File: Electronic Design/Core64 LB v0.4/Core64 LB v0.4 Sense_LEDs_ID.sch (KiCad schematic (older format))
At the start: 18 parts, among them J6 Conn_01x08_Female, U3 LM393, U5 74HC02, U7 LM393

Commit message: Update schematic
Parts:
- added C4, C5: 0.1uF, Capacitor_SMD:C_0805_2012Metric, symbol Device:C
- added J10: TSM-106-03-T-DV‎, Connector_PinHeader_2.54mm:PinHeader_2x07_P2.54mm_Vertical_SMD_and_TH, symbol Connector_Generic:Conn_02x07_Odd_Even
- added J17: LED Cur. Mon., Connector_PinSocket_2.54mm:PinSocket_1x02_P2.54mm_Vertical, symbol Connector_Generic:Conn_01x02
- added R50: 470, Resistor_SMD:R_0805_2012Metric, symbol Device:R
- added U3: SN74LV1T125DBVR, Package_TO_SOT_SMD:SOT-23-5, symbol Logic_LevelTranslator:SN74LV1T125DBVR
- added U4: M24C01-RMN, Package_SO:SOIC-8_3.9x4.9mm_P1.27mm, symbol Memory_EEPROM:M24C01-RMN
- J6: value Conn_01x08_Female -> HEADER_8-PIN_0.1
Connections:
- net 3V3: now also C5.1, U4.1 (E0), U4.2 (E1), U4.3 (E2), U4.8 (VCC)
- net GNDD: now also C4.2, C5.2, U3.1 (/OE), U3.3 (GND), U4.4 (VSS), U4.7 (~WC)
- new net: R50.2, U3.4 (Y)
- new net 5V0: C4.1, J10.2 (Pin_2), J17.1 (Pin_1), J17.2 (Pin_2), U3.5 (VCC)
- new net GND: J10.9 (Pin_9)
- new net I2C_CLOCK: U4.6 (SCL)
- new net I2C_DATA: U4.5 (SDA)
- new net LED_ARRAY_3V3_SIG: U3.2 (A)
- new net LED_ARRAY_5V0_SIG: J10.12 (Pin_12), R50.1
- no-connect marks 0 -> 11
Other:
- note added: "BOARD ID AND S/N"
- note added: "EEPROM I2C ADDRESS: 0b1010111, 0x57 (87)"
- note added: "Header not populated"
- note added: "LED ARRAY DRIVE AND LEVEL SHIFT"
- note added: "SENSE DEBUG"
- note added: "SENSE SIGNAL DIFFERENTIAL AMPLIFIERS"
- note added: "SILKSCREEN: 3V3 ONLY\nSENSE DEBUG"
- note added: "SILKSCREEN: \n5V0 ONLY\nLED ARRAY"
- note added: "TSM-106 (2x6) required\nTSM-107 (2x7) alternate"
- note removed: "SENSE DEBUG SOCKET"
- note removed: "SENSE SIGNAL PROCESSING"
- note removed: "SILKSCREEN: 3V3 ONLY\nSENSE PORT"
- moved on the sheet: J6

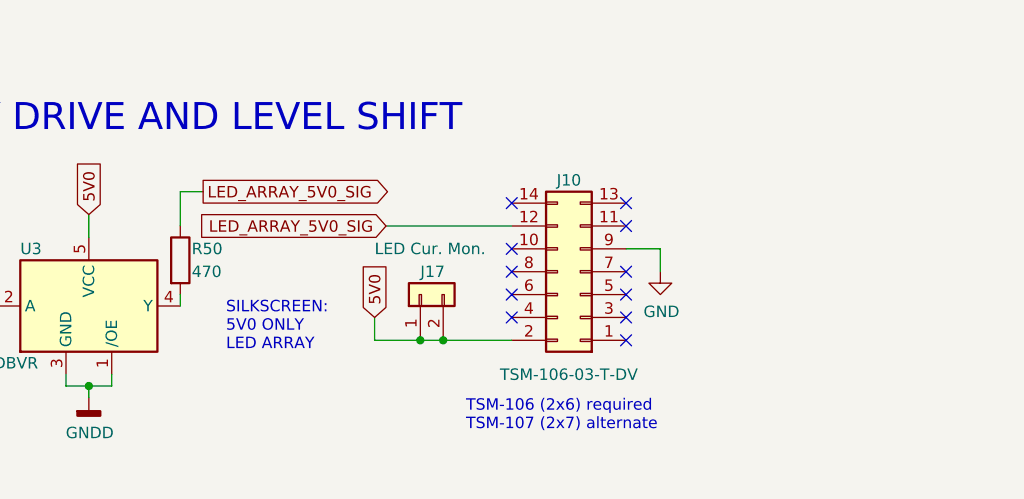
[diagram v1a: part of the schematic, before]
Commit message: Update footprint mounting holes TFT, LED array, battery packs, lipo charger, arrange components to fit on the board
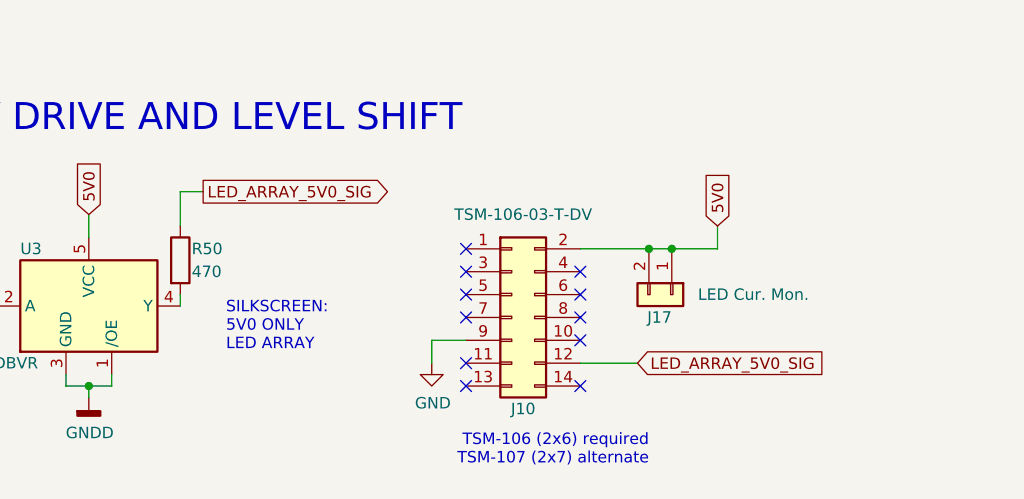
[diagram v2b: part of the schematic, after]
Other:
- moved on the sheet: J10, J17
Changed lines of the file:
@@
 Wire Wire Line
 	2300 5650 2300 5500
-NoConn ~ 3750 5550
-NoConn ~ 4250 5550
-Text Notes 3550 6550 0    50   ~ 0
+NoConn ~ 4050 6350
+NoConn ~ 3550 6350
+Text Notes 4350 6700 2    50   ~ 0
 TSM-106 (2x6) required\nTSM-107 (2x7) alternate
 Text Notes 2500 6200 0    50   ~ 0
 SILKSCREEN: \n5V0 ONLY\nLED ARRAY
 Wire Wire Line
-	3150 6050 3150 6150
-Text GLabel 3150 6050 1    50   Input ~ 0
+	4650 5650 4650 5750
+Text GLabel 4650 5650 1    50   Input ~ 0
 5V0
-NoConn ~ 4250 6150
-NoConn ~ 4250 6050
-NoConn ~ 4250 5950
-NoConn ~ 4250 5850
-NoConn ~ 4250 5650
-NoConn ~ 3750 5750
-NoConn ~ 3750 5850
-NoConn ~ 3750 5950
-NoConn ~ 3750 6050
-Wire Wire Line
-	4400 5750 4400 5850
-Wire Wire Line
-	4250 5750 4400 5750
-Wire Wire Line
-	3750 5650 3200 5650
-Wire Wire Line
-	3750 6150 3450 6150
+NoConn ~ 3550 5750
+NoConn ~ 3550 5850
+NoConn ~ 3550 5950
+NoConn ~ 3550 6050
+NoConn ~ 3550 6250
+NoConn ~ 4050 6150
+NoConn ~ 4050 6050
+NoConn ~ 4050 5950
+NoConn ~ 4050 5850
+Wire Wire Line
+	3400 6150 3400 6250
+Wire Wire Line
+	3550 6150 3400 6150
+Wire Wire Line
+	4050 6250 4300 6250
+Wire Wire Line
+	4050 5750 4350 5750
 $Comp
 L power:GND #PWR?
 U 1 1 5F7F8247
-P 4400 5850
+P 3400 6250
 AR Path="/5E755787/5F7F8247" Ref="#PWR?"  Part="1"
 AR Path="/5F7F8247" Ref="#PWR?"  Part="1"
 AR Path="/5E75D6AB/5F7F8247" Ref="#PWR0114"  Part="1"
-F 0 "#PWR0114" H 4400 5600 50  0001 C CNN
-F 1 "GND" H 4405 5675 50  0000 C CNN
-F 2 "" H 4400 5850 50  0001 C CNN
-F 3 "" H 4400 5850 50  0001 C CNN
-	1    4400 5850
-	1    0    0    -1
-$EndComp
-Text GLabel 3200 5650 0    50   Input ~ 0
+F 0 "#PWR0114" H 3400 6000 50  0001 C CNN
+F 1 "GND" H 3405 6075 50  0000 C CNN
+F 2 "" H 3400 6250 50  0001 C CNN
+F 3 "" H 3400 6250 50  0001 C CNN
+	1    3400 6250
+	1    0    0    -1
+$EndComp
+Text GLabel 4300 6250 2    50   Input ~ 0
 LED_ARRAY_5V0_SIG
 $Comp
 L Connector_Generic:Conn_02x07_Odd_Even J?
 U 1 1 5F7F824E
-P 4050 5850
+P 3750 6050
 AR Path="/5F7F824E" Ref="J?"  Part="1"
 AR Path="/5E75D6AB/5F7F824E" Ref="J10"  Part="1"
-F 0 "J10" H 4100 5450 50  0000 C CNN
-F 1 "TSM-106-03-T-DV‎" H 4100 6300 50  0000 C CNN
-F 2 "Connector_PinHeader_2.54mm:PinHeader_2x07_P2.54mm_Vertical_SMD_and_TH" H 4050 5850 50  0001 C CNN
-F 3 "~" H 4050 5850 50  0001 C CNN
-	1    4050 5850
-	-1   0    0    1
+F 0 "J10" H 3800 5650 50  0000 C CNN
+F 1 "TSM-106-03-T-DV‎" H 3800 6500 50  0000 C CNN
+F 2 "Connector_PinHeader_2.54mm:PinHeader_2x07_P2.54mm_Vertical_SMD_and_TH" H 3750 6050 50  0001 C CNN
+F 3 "~" H 3750 6050 50  0001 C CNN
+	1    3750 6050
+	1    0    0    -1
 $EndComp
 $Comp
@@
 L Connector_Generic:Conn_01x02 J?
 U 1 1 5F951C5C
-P 3350 5950
+P 4450 5950
 AR Path="/5E7548ED/5F951C5C" Ref="J?"  Part="1"
 AR Path="/5E75D6AB/5F951C5C" Ref="J17"  Part="1"
-F 0 "J17" V 3450 5950 50  0000 R CNN
-F 1 "LED Cur. Mon." V 3550 6150 50  0000 R CNN
-F 2 "Connector_PinSocket_2.54mm:PinSocket_1x02_P2.54mm_Vertical" H 3350 5950 50  0001 C CNN
-F 3 "~" H 3350 5950 50  0001 C CNN
-	1    3350 5950
-	0    -1   -1   0
-$EndComp
-Wire Wire Line
-	3350 6150 3450 6150
-Connection ~ 3350 6150
-Wire Wire Line
-	3350 6150 3150 6150
-Connection ~ 3450 6150
+F 0 "J17" V 4550 5950 50  0000 R CNN
+F 1 "LED Cur. Mon." V 4450 6550 50  0000 R CNN
+F 2 "Connector_PinSocket_2.54mm:PinSocket_1x02_P2.54mm_Vertical" H 4450 5950 50  0001 C CNN
+F 3 "~" H 4450 5950 50  0001 C CNN
+	1    4450 5950
+	0    1    1    0
+$EndComp
+Wire Wire Line
+	4450 5750 4350 5750
+Connection ~ 4450 5750
+Wire Wire Line
+	4450 5750 4650 5750
+Connection ~ 4350 5750
 $EndSCHEMATC

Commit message: Clean up and tweek LB schematics
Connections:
- net 3V3: now also J10.1 (Pin_1)
- net 5V0: now also J10.4 (Pin_4)
- net GND: now also J10.14 (Pin_14), J10.6 (Pin_6)
- no-connect marks 11 -> 7
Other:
- note added: "TSM-106 (2x6) required\nTSM-107 (2x7) alternate\n\nSymbol view is looking down\non the front face of the Logic\nBoard, with the male header\npins pointing up at you."
- note removed: "TSM-106 (2x6) required\nTSM-107 (2x7) alternate"
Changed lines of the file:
@@
 Wire Wire Line
 	2300 5650 2300 5500
-NoConn ~ 4050 6350
 NoConn ~ 3550 6350
-Text Notes 4350 6700 2    50   ~ 0
-TSM-106 (2x6) required\nTSM-107 (2x7) alternate
+Text Notes 3350 7200 0    50   ~ 0
+TSM-106 (2x6) required\nTSM-107 (2x7) alternate\n\nSymbol view is looking down\non the front face of the Logic\nBoard, with the male header\npins pointing up at you.
 Text Notes 2500 6200 0    50   ~ 0
 SILKSCREEN: \n5V0 ONLY\nLED ARRAY
@@
 Text GLabel 4650 5650 1    50   Input ~ 0
 5V0
-NoConn ~ 3550 5750
 NoConn ~ 3550 5850
 NoConn ~ 3550 5950
@@
 NoConn ~ 4050 6150
 NoConn ~ 4050 6050
-NoConn ~ 4050 5950
-NoConn ~ 4050 5850
 Wire Wire Line
 	3400 6150 3400 6250
@@
 	4050 6250 4300 6250
 Wire Wire Line
-	4050 5750 4350 5750
+	4050 5750 4150 5750
 $Comp
 L power:GND #PWR?
@@
 	4450 5750 4650 5750
 Connection ~ 4350 5750
+Text GLabel 3450 5750 0    50   Input ~ 0
+3V3
+Wire Wire Line
+	3450 5750 3550 5750
+Wire Wire Line
+	4050 5850 4150 5850
+Wire Wire Line
+	4150 5850 4150 5750
+Connection ~ 4150 5750
+Wire Wire Line
+	4150 5750 4350 5750
+Wire Wire Line
+	4050 5950 4150 5950
+Wire Wire Line
+	4150 5950 4150 6350
+Wire Wire Line
+	4150 6350 4050 6350
+$Comp
+L power:GND #PWR?
+U 1 1 5FB058FB
+P 4150 6350
+AR Path="/5E755787/5FB058FB" Ref="#PWR?"  Part="1"
+AR Path="/5FB058FB" Ref="#PWR?"  Part="1"
+AR Path="/5E75D6AB/5FB058FB" Ref="#PWR0107"  Part="1"
+F 0 "#PWR0107" H 4150 6100 50  0001 C CNN
+F 1 "GND" H 4155 6175 50  0000 C CNN
+F 2 "" H 4150 6350 50  0001 C CNN
+F 3 "" H 4150 6350 50  0001 C CNN
+	1    4150 6350
+	1    0    0    -1
+$EndComp
+Connection ~ 4150 6350
 $EndSCHEMATC

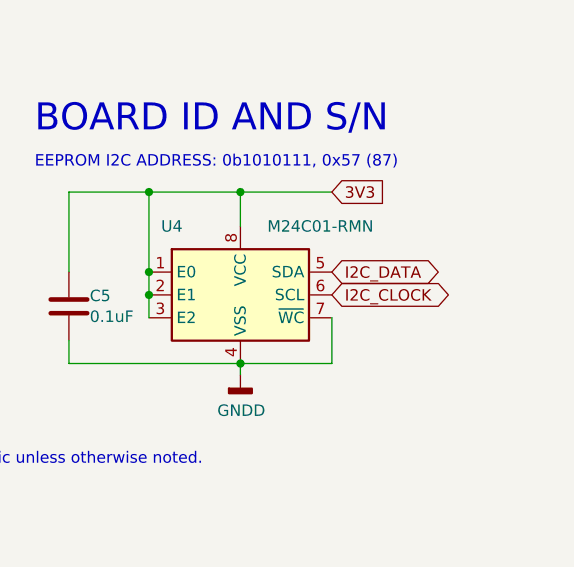
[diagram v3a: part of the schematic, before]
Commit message: Route bottom edge area EEPROM, QWIIC, SAO, BAT MON, I2C PULL-UPS
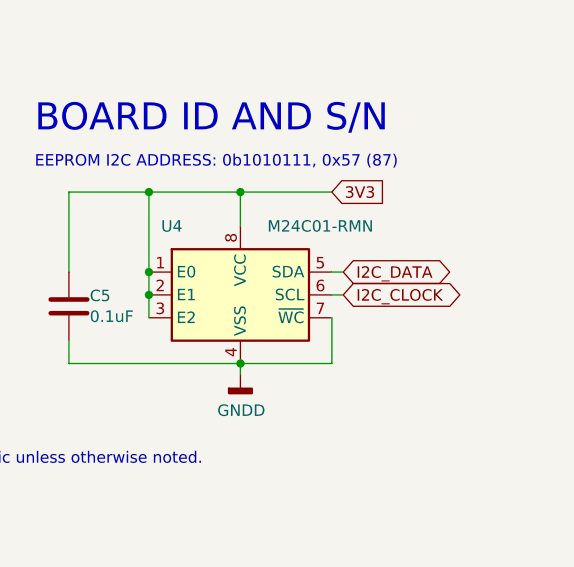
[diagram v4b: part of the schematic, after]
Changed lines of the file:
@@
 	1    0    0    -1
 $EndComp
-Text GLabel 9500 5900 2    50   BiDi ~ 0
+Text GLabel 9550 5900 2    50   BiDi ~ 0
 I2C_DATA
-Text GLabel 9500 6000 2    50   BiDi ~ 0
+Text GLabel 9550 6000 2    50   BiDi ~ 0
 I2C_CLOCK
 Text GLabel 9500 5550 2    50   Input ~ 0
@@
 $EndComp
 Connection ~ 4150 6350
+Wire Wire Line
+	9500 5900 9550 5900
+Wire Wire Line
+	9500 6000 9550 6000
 $EndSCHEMATC

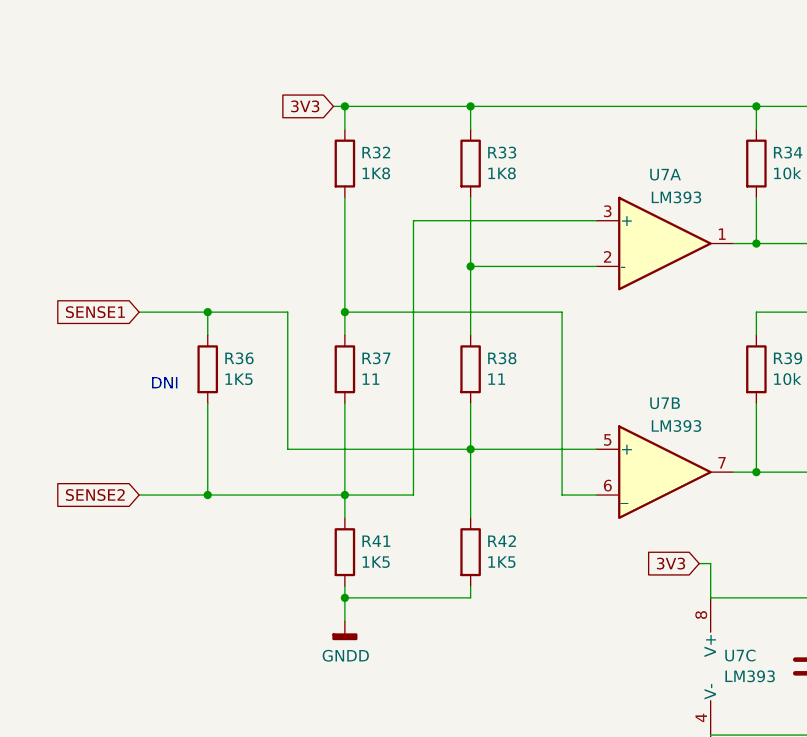
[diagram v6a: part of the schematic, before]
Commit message: Organize BOM and build order to prototype V0.4 LB
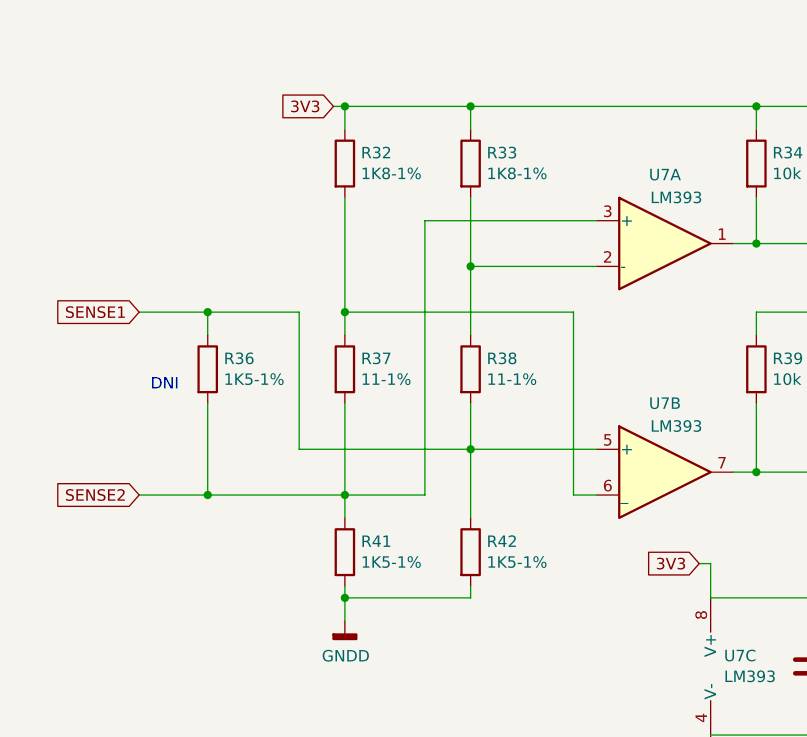
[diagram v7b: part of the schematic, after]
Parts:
- R32, R33: value 1K8 -> 1K8-1%
- R36, R41, R42: value 1K5 -> 1K5-1%
- R37, R38: value 11 -> 11-1%
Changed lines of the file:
@@
 P 1850 1700
 F 0 "R32" H 1920 1746 50  0000 L CNN
-F 1 "1K8" H 1920 1655 50  0000 L CNN
+F 1 "1K8-1%" H 1920 1655 50  0000 L CNN
 F 2 "Resistor_SMD:R_0805_2012Metric" V 1780 1700 50  0001 C CNN
 F 3 "~" H 1850 1700 50  0001 C CNN
@@
 P 2400 1700
 F 0 "R33" H 2470 1746 50  0000 L CNN
-F 1 "1K8" H 2470 1655 50  0000 L CNN
+F 1 "1K8-1%" H 2470 1655 50  0000 L CNN
 F 2 "Resistor_SMD:R_0805_2012Metric" V 2330 1700 50  0001 C CNN
 F 3 "~" H 2400 1700 50  0001 C CNN
@@
 P 1850 2600
 F 0 "R37" H 1920 2646 50  0000 L CNN
-F 1 "11" H 1920 2555 50  0000 L CNN
+F 1 "11-1%" H 1920 2555 50  0000 L CNN
 F 2 "Resistor_SMD:R_0805_2012Metric" V 1780 2600 50  0001 C CNN
 F 3 "~" H 1850 2600 50  0001 C CNN
@@
 P 2400 2600
 F 0 "R38" H 2470 2646 50  0000 L CNN
-F 1 "11" H 2470 2555 50  0000 L CNN
+F 1 "11-1%" H 2470 2555 50  0000 L CNN
 F 2 "Resistor_SMD:R_0805_2012Metric" V 2330 2600 50  0001 C CNN
 F 3 "~" H 2400 2600 50  0001 C CNN
@@
 P 1850 3400
 F 0 "R41" H 1920 3446 50  0000 L CNN
-F 1 "1K5" H 1920 3355 50  0000 L CNN
+F 1 "1K5-1%" H 1920 3355 50  0000 L CNN
 F 2 "Resistor_SMD:R_0805_2012Metric" V 1780 3400 50  0001 C CNN
 F 3 "~" H 1850 3400 50  0001 C CNN
@@
 	950  2350 1250 2350
 Wire Wire Line
-	1600 2350 1600 2950
-Wire Wire Line
-	1600 2950 2400 2950
+	1650 2350 1650 2950
+Wire Wire Line
+	1650 2950 2400 2950
 Connection ~ 2400 2950
 Wire Wire Line
@@
 	2400 2150 2400 2450
 Wire Wire Line
-	2950 1950 2150 1950
-Wire Wire Line
-	2150 1950 2150 3150
-Wire Wire Line
-	2150 3150 1850 3150
-Wire Wire Line
-	2800 3150 2950 3150
-Wire Wire Line
-	1850 2350 2800 2350
+	2950 1950 2200 1950
+Wire Wire Line
+	2200 1950 2200 3150
+Wire Wire Line
+	2200 3150 1850 3150
+Wire Wire Line
+	2850 3150 2950 3150
+Wire Wire Line
+	1850 2350 2850 2350
 Connection ~ 1850 2350
 Wire Wire Line
@@
 Connection ~ 1250 2350
 Wire Wire Line
-	1250 2350 1600 2350
+	1250 2350 1650 2350
 Wire Wire Line
 	1250 2750 1250 3150
@@
 P 1250 2600
 F 0 "R36" H 1320 2646 50  0000 L CNN
-F 1 "1K5" H 1320 2555 50  0000 L CNN
+F 1 "1K5-1%" H 1320 2555 50  0000 L CNN
 F 2 "Resistor_SMD:R_0805_2012Metric" V 1180 2600 50  0001 C CNN
 F 3 "~" H 1250 2600 50  0001 C CNN
@@
 $EndComp
 Wire Wire Line
-	2800 2350 2800 3150
+	2850 2350 2850 3150
 Connection ~ 3650 2050
 Wire Wire Line
@@
 P 2400 3400
 F 0 "R42" H 2470 3446 50  0000 L CNN
-F 1 "1K5" H 2470 3355 50  0000 L CNN
+F 1 "1K5-1%" H 2470 3355 50  0000 L CNN
 F 2 "Resistor_SMD:R_0805_2012Metric" V 2330 3400 50  0001 C CNN
 F 3 "~" H 2400 3400 50  0001 C CNN
